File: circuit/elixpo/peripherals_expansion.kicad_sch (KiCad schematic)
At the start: 21 parts, among them J4 MicroSD SPI, J5 I2C / accessory, Q1 MMBT2222A, U7 MPU-6050, U8 TSOP38238, U9 WS2812B-2020

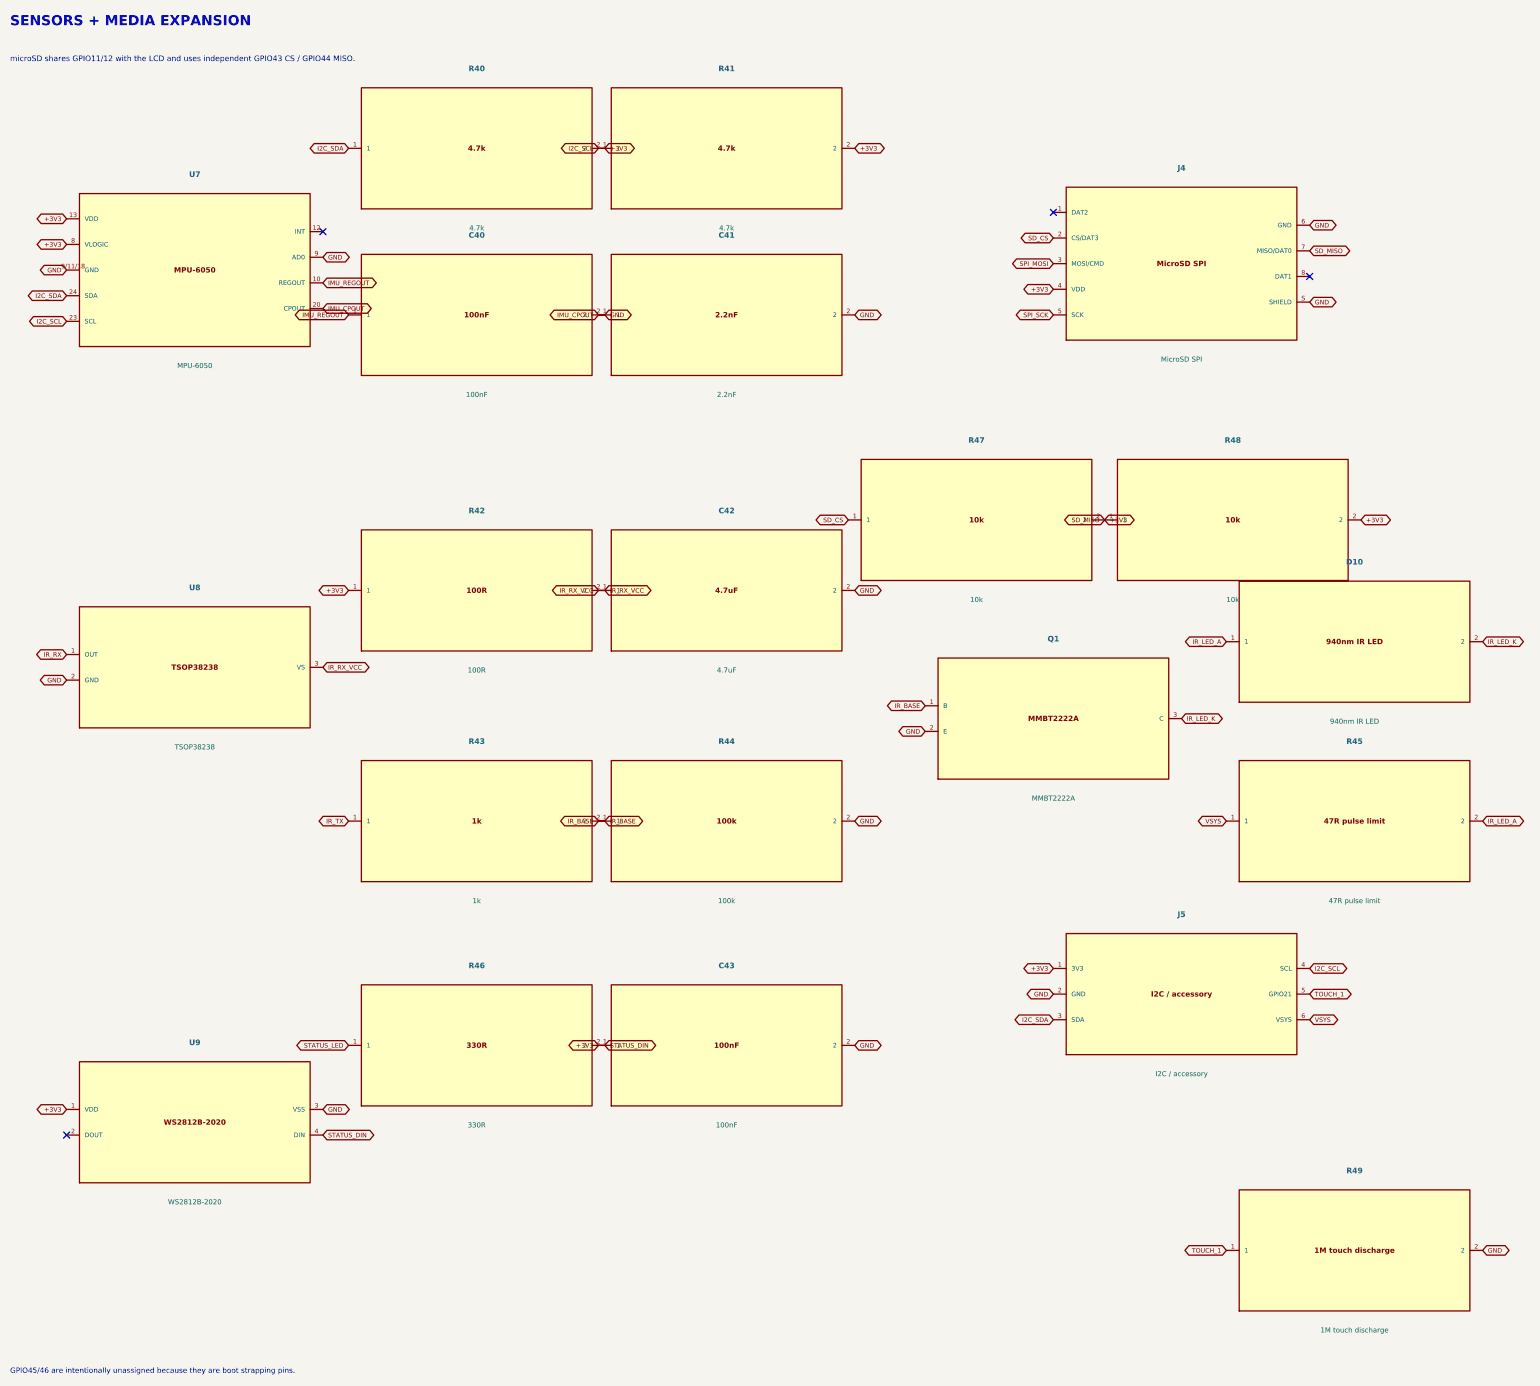
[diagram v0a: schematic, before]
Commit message: feat(hardware): complete badge schematic and procurement BOM
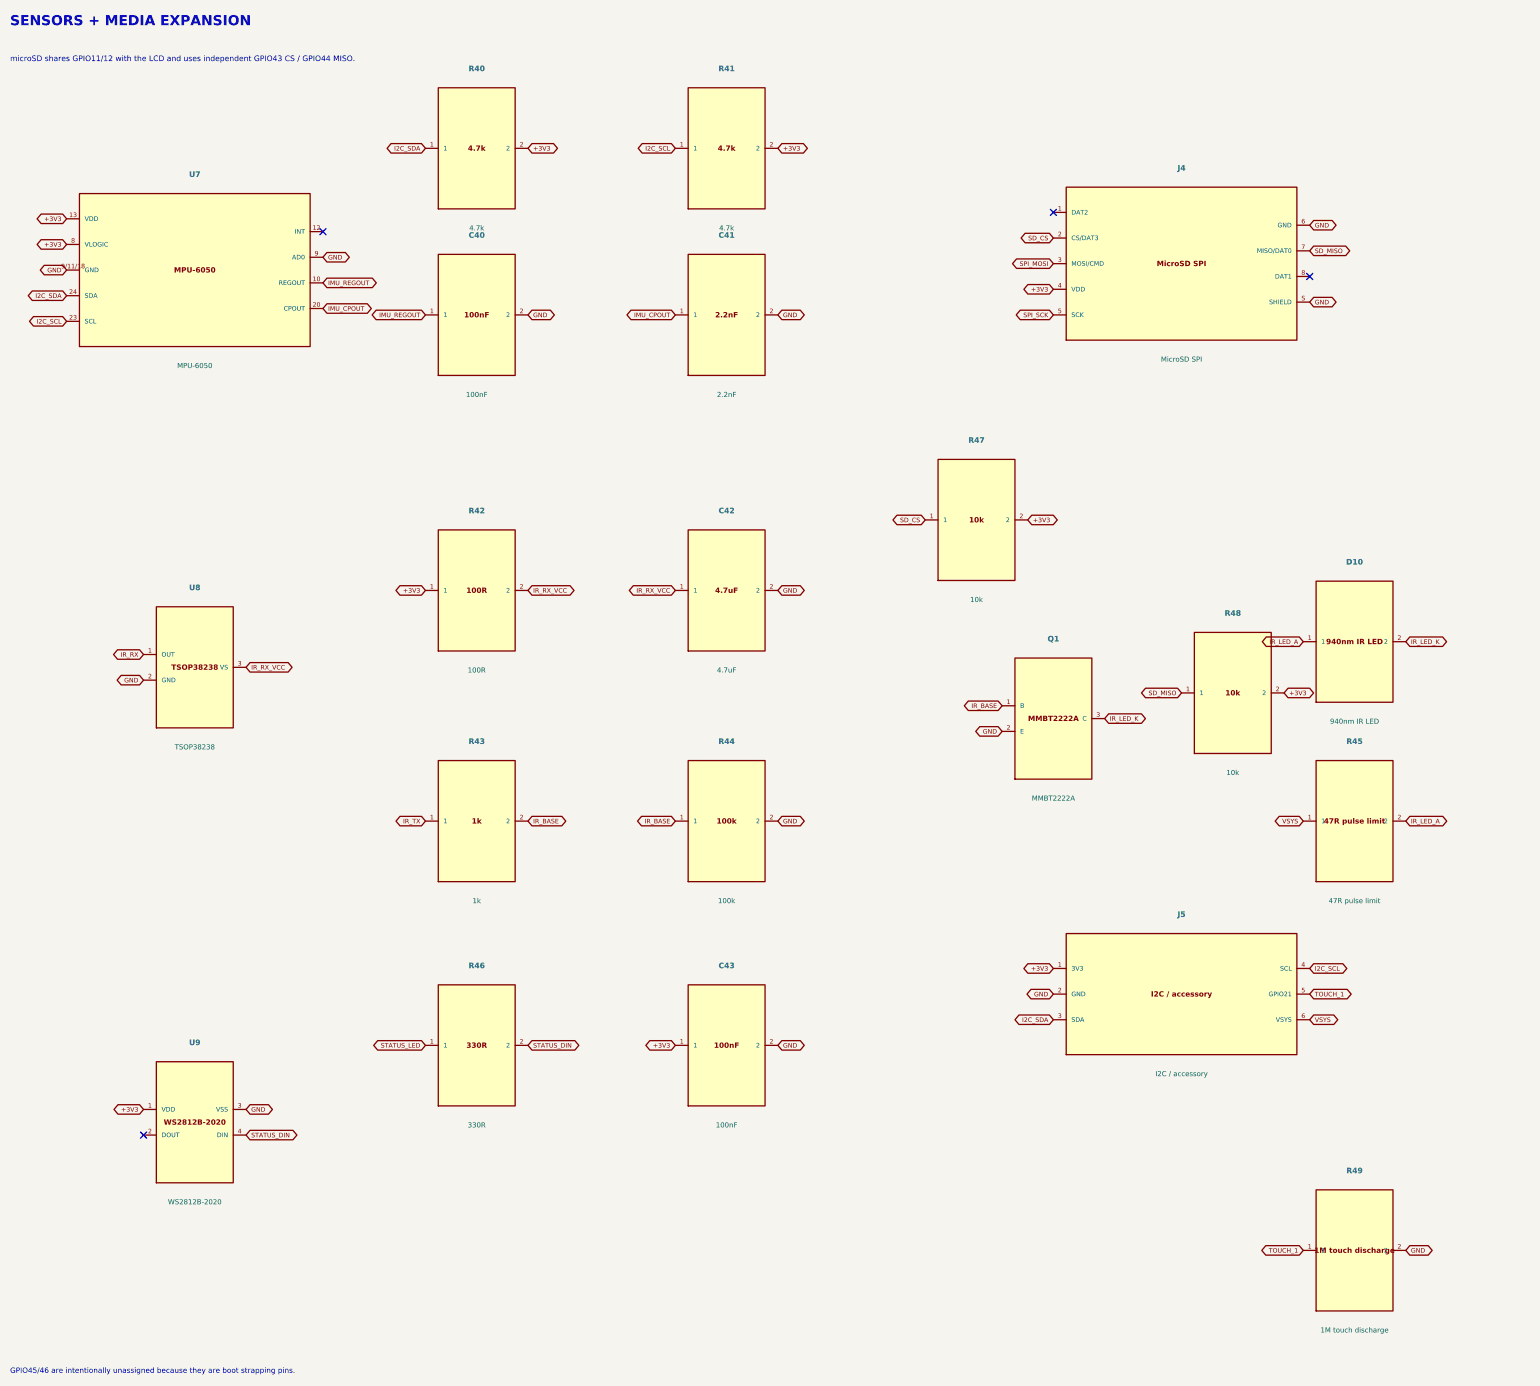
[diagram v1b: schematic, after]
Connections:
- net +3V3: no longer J4.7 (MISO/DAT0), R48.1
- new net SD_MISO: J4.7 (MISO/DAT0), R48.1
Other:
- moved on the sheet: R48
